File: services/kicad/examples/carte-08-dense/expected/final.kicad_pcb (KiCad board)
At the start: 2 copper layers, 125 x 95 mm, 56 parts, among them J1 IN_5V, J2 SWD, J3 IO0, J4 IO1, J5 IO2, J6 IO3, J7 IO4, U1 STM32F103C8T6, U2 AMS1117-3.3

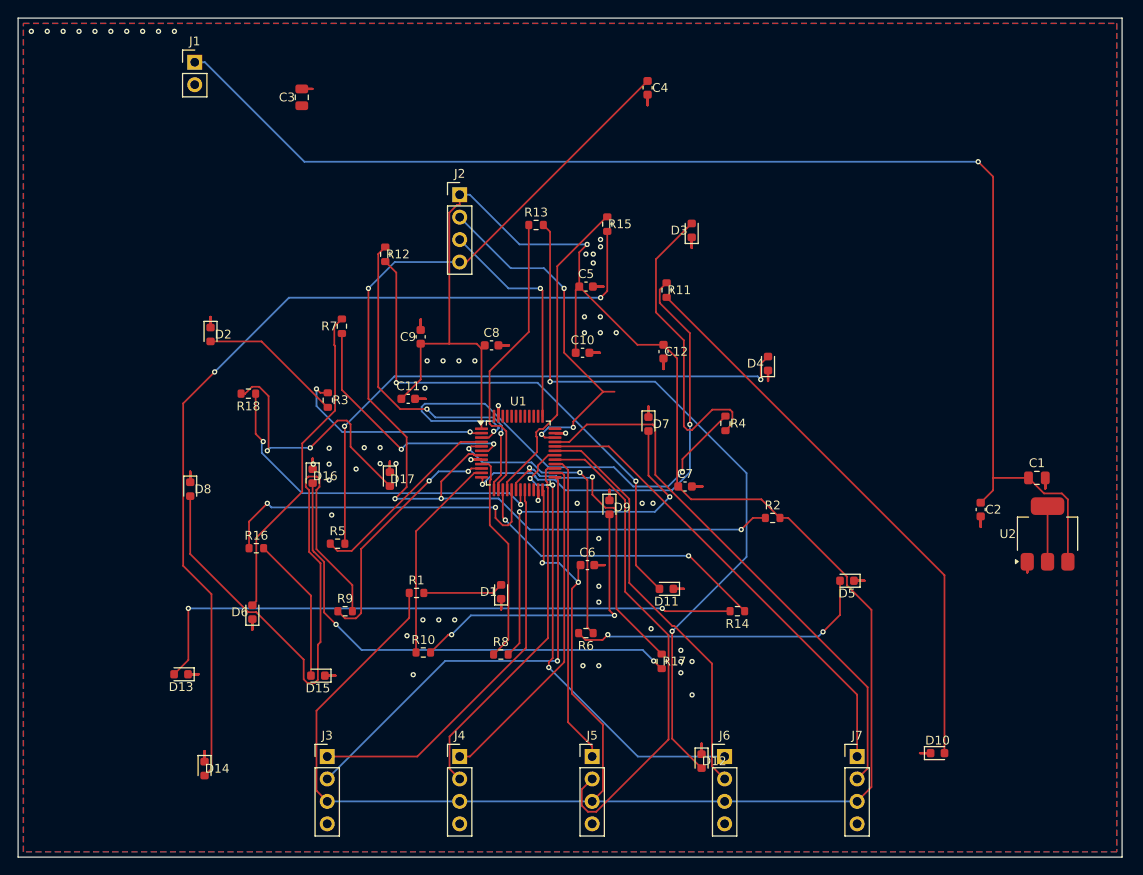
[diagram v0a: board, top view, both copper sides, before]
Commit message: feat(kicad): placement pro et routage 100 % fabricable sur les 16 cartes -- integration sur main (#164)
Branche d'integration coupee depuis origin/main (fab2a82, PR #162) : les
fichiers cles de main etaient des instantanes de feat/placement-seed-snap-
bypass (routing.py = 7981019, placement.py = 437a8b4...). On reprend donc
l'arbre entier de cette branche (345 commits, dernier 9f48667) et on y
conserve ce que main seul apportait :
- tools/verrou_routage.py + son test : « 6,2 Go par routage » rectifie
  (0,2 Go mesure ; c'est la concurrence qui emballe la memoire) ;
- tests/test_driver_llm_resync.py ;
- CLAUDE.md, PLAN.md, DECISIONS.md : fusion a trois voies, les sections
  des deux lignes conservees (2026-09-05 conteneur/verrou, 2026-09-07
  parcours asynchrone et chaine du driver, 2026-09-09/10 lecons).
Les skills *-delegate restent supprimes (remplaces le 2026-08-30).

Contenu : banc en deux phases (placement valide puis routage gele), snap
sur les regles natives, repli GND cible, journal Freerouting incremental,
horloge sans progres, via d'echappement vers le plan principal,
serigraphie degagee ; 16 cartes livrees a 100 %, 0 erreur DRC.

Verification : pytest services/kicad 1805 passed, 16 skipped ;
pnpm type-check 8/8.


Claude-Session: https://claude.ai/code/session_01TnMqm4La2CxQHHB5K8aSSV

Co-authored-by: Claude Fable 5.1 <noreply@anthropic.com>
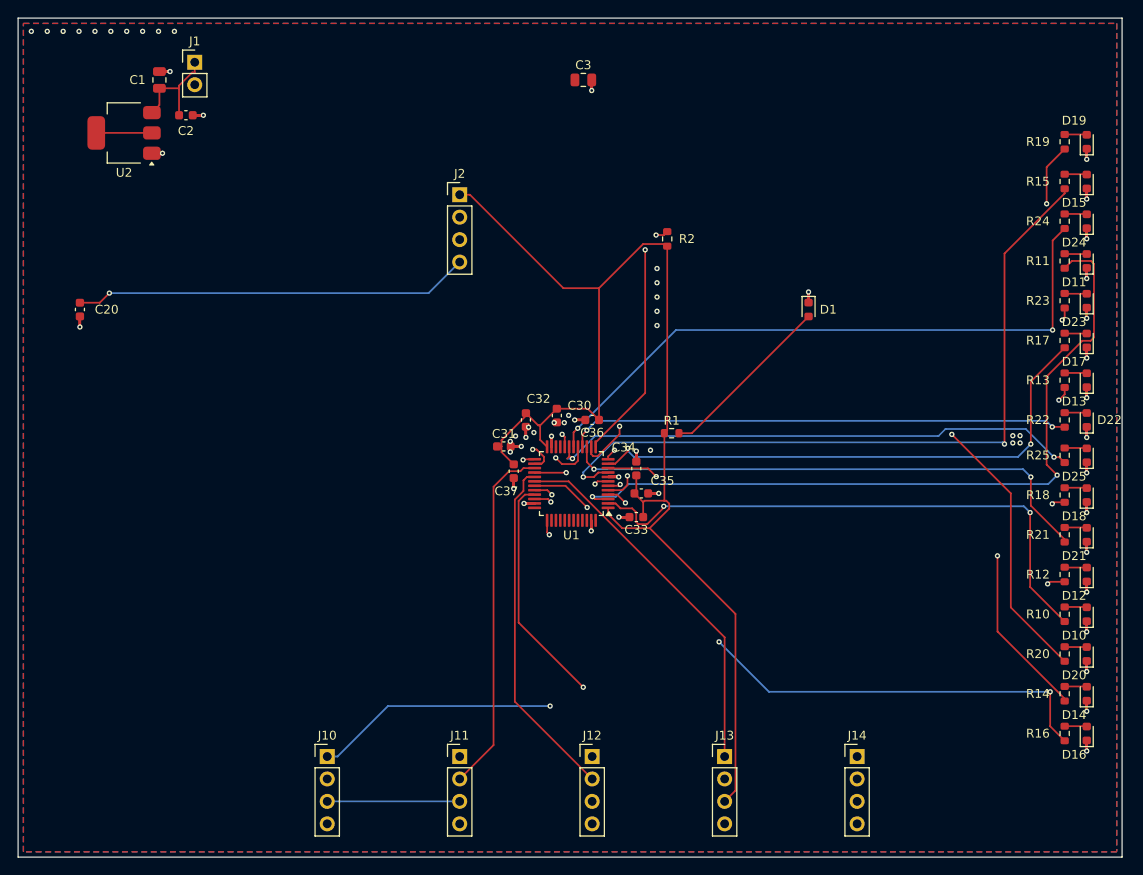
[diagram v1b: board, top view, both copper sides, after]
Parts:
- removed C10, C11, C12, C4, C5, C6, C7, C8, C9: 100nF, C_0603_1608Metric
- removed D2, D3, D4, D5, D6, D7, D8, D9: LED, LED_0603_1608Metric
- removed J3: IO0, PinHeader_1x04_P2.54mm_Vertical
- removed J4: IO1, PinHeader_1x04_P2.54mm_Vertical
- removed J5: IO2, PinHeader_1x04_P2.54mm_Vertical
- removed J6: IO3, PinHeader_1x04_P2.54mm_Vertical
- removed J7: IO4, PinHeader_1x04_P2.54mm_Vertical
- removed R3, R4, R5, R6, R7, R8, R9: 1k, R_0603_1608Metric
- added C20: 100nF, C_0603_1608Metric, F.Cu at (93.0, 90.5)
- added C30: 100nF, C_0603_1608Metric, F.Cu at (147.0, 102.5)
- added C31: 100nF, C_0603_1608Metric, F.Cu at (141.0, 106.0)
- added C32: 100nF, C_0603_1608Metric, F.Cu at (143.5, 103.0)
- added C33: 100nF, C_0603_1608Metric, F.Cu at (156.0, 114.0)
- added C34: 100nF, C_0603_1608Metric, F.Cu at (156.0, 108.5)
- added C35: 100nF, C_0603_1608Metric, F.Cu at (156.6, 111.3)
- added C36: 100nF, C_0603_1608Metric, F.Cu at (151.0, 103.0)
- added C37: 100nF, C_0603_1608Metric, F.Cu at (142.1, 108.8)
- added D18: LED, LED_0603_1608Metric, F.Cu at (207.0, 111.5)
- added D19: LED, LED_0603_1608Metric, F.Cu at (207.0, 71.5)
- added D20: LED, LED_0603_1608Metric, F.Cu at (207.0, 129.5)
- added D21: LED, LED_0603_1608Metric, F.Cu at (207.0, 116.0)
- added D22: LED, LED_0603_1608Metric, F.Cu at (207.0, 103.0)
- added D23: LED, LED_0603_1608Metric, F.Cu at (207.0, 89.5)
- added D24: LED, LED_0603_1608Metric, F.Cu at (207.0, 80.5)
- added D25: LED, LED_0603_1608Metric, F.Cu at (207.0, 107.0)
- added J10: IO0, PinHeader_1x04_P2.54mm_Vertical, F.Cu at (121.0, 141.1)
- added J11: IO1, PinHeader_1x04_P2.54mm_Vertical, F.Cu at (136.0, 141.1)
- added J12: IO2, PinHeader_1x04_P2.54mm_Vertical, F.Cu at (151.0, 141.1)
- added J13: IO3, PinHeader_1x04_P2.54mm_Vertical, F.Cu at (166.0, 141.1)
- added J14: IO4, PinHeader_1x04_P2.54mm_Vertical, F.Cu at (181.0, 141.1)
- added R19: 1k, R_0603_1608Metric, F.Cu at (204.5, 71.5)
- added R20: 1k, R_0603_1608Metric, F.Cu at (204.5, 129.5)
- added R21: 1k, R_0603_1608Metric, F.Cu at (204.5, 116.0)
- added R22: 1k, R_0603_1608Metric, F.Cu at (204.5, 103.0)
- added R23: 1k, R_0603_1608Metric, F.Cu at (204.5, 89.5)
- added R24: 1k, R_0603_1608Metric, F.Cu at (204.5, 80.5)
- added R25: 1k, R_0603_1608Metric, F.Cu at (204.5, 107.0)
- moved U2 114.0 mm to (98.0, 70.5), turned to 180 degrees
- moved C1 109.1 mm to (102.0, 64.5), turned to 90 degrees
- moved D13 107.8 mm to (207.0, 98.5), turned to 90 degrees
- moved D15 103.5 mm to (207.0, 76.0), turned to 90 degrees
- moved C2 100.5 mm to (105.0, 68.5), turned to 0 degrees
- moved D14 100.2 mm to (207.0, 134.0), turned to 90 degrees
- moved R16 93.9 mm to (204.5, 138.5), turned to 90 degrees
- moved R18 93.1 mm to (204.5, 111.5), turned to 90 degrees
- moved D16 92.4 mm to (207.0, 138.5), turned to 90 degrees
- moved R12 85.0 mm to (204.5, 120.5), turned to 90 degrees
- moved D17 80.5 mm to (207.0, 94.0), turned to 90 degrees
- moved R10 72.7 mm to (204.5, 125.0), turned to 90 degrees
- moved R13 62.4 mm to (204.5, 98.5), turned to 90 degrees
- moved D11 60.4 mm to (207.0, 85.0), turned to 90 degrees
- moved R17 58.3 mm to (204.5, 94.0), turned to 90 degrees
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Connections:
- D10 pad 2: LEDA8 -> LEDA0
- D11 pad 2: LEDA9 -> LEDA1
- D12 pad 2: LEDA10 -> LEDA2
- D13 pad 2: LEDA11 -> LEDA3
- D14 pad 2: LEDA12 -> LEDA4
- D15 pad 2: LEDA13 -> LEDA5
- D16 pad 2: LEDA14 -> LEDA6
- D17 pad 2: LEDA15 -> LEDA7
- R10 pad 1: IO_L7 -> IO_L0
- R10 pad 2: LEDA7 -> LEDA0
- R11 pad 1: IO_L8 -> IO_L1
- R11 pad 2: LEDA8 -> LEDA1
- R12 pad 1: IO_L9 -> IO_L2
- R12 pad 2: LEDA9 -> LEDA2
- R13 pad 1: IO_L10 -> IO_L3
- R13 pad 2: LEDA10 -> LEDA3
- R14 pad 1: IO_L11 -> IO_L4
- R14 pad 2: LEDA11 -> LEDA4
- R15 pad 1: IO_L12 -> IO_L5
- R15 pad 2: LEDA12 -> LEDA5
- R16 pad 1: IO_L13 -> IO_L6
- R16 pad 2: LEDA13 -> LEDA6
- R17 pad 1: IO_L14 -> IO_L7
- R17 pad 2: LEDA14 -> LEDA7
- R18 pad 1: IO_L15 -> IO_L8
- R18 pad 2: LEDA15 -> LEDA8
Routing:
- net VIN: track 149.8 -> 12.2 mm, vias 1 -> 0
- net LEDA12: track 103.8 -> 2.52 mm, vias 2 -> 0
- net GND: track 122.4 -> 208.8 mm, vias 58 -> 61
- net LEDA10: track 82.9 -> 2.52 mm, vias 2 -> 0
- net +3V3: track 281.5 -> 208.4 mm, vias 3 -> 0
- net LEDA6: track 70.6 -> 2.52 mm
- net LEDA11: track 69.6 -> 2.52 mm, vias 2 -> 0
- net LEDA2: track 65.9 -> 2.52 mm, vias 2 -> 0
- net LEDA8: track 64.6 -> 2.52 mm
- net IO_L5: track 24.1 -> 84.5 mm, vias 0 -> 2
- net LEDA9: track 59.3 -> 2.52 mm, vias 2 -> 0
- net LEDA14: track 56.1 -> 2.52 mm, vias 2 -> 0
- net IO_L6: track 27.9 -> 73.6 mm, vias 2 -> 3
- net IO_L10: track 33.6 -> 75.1 mm, vias 0 -> 2
- net IO_L0: track 23.4 -> 64.6 mm
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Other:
- copper layers 2 -> 4

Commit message: chore(banc): relivrer carte-01..10 avec la couture corrigee
Boards reroutes par HTTP depuis placement.kicad_pcb inchange, avec le
code de #217. Juges par remesurer_banc.py : 0 erreur, 0 connexion
manquante sur les dix. 678 -> 443 vias ; la rangee de vias GND du bord
haut a disparu.

mesures.json : `board` recompte, `drc_du_board` rejuge, nouvelle cle
`couture_corrigee` (date, vias_avant, couches). journal.txt et les
champs du run d origine sont laisses tels quels et le disent.
rendu-3d.png : kicad-cli, modeles 3D, iso 1400x900.

Couches d un tirage : huit cartes sur 2, carte-08 et carte-10 sur 4.
CLAUDE.md et BANC_DRIVER_LLM.md recomptes. carte-11 non touchee.

Co-Authored-By: Claude Opus 5 (1M context) <noreply@anthropic.com>
Claude-Session: https://claude.ai/code/session_01TnMqm4La2CxQHHB5K8aSSV
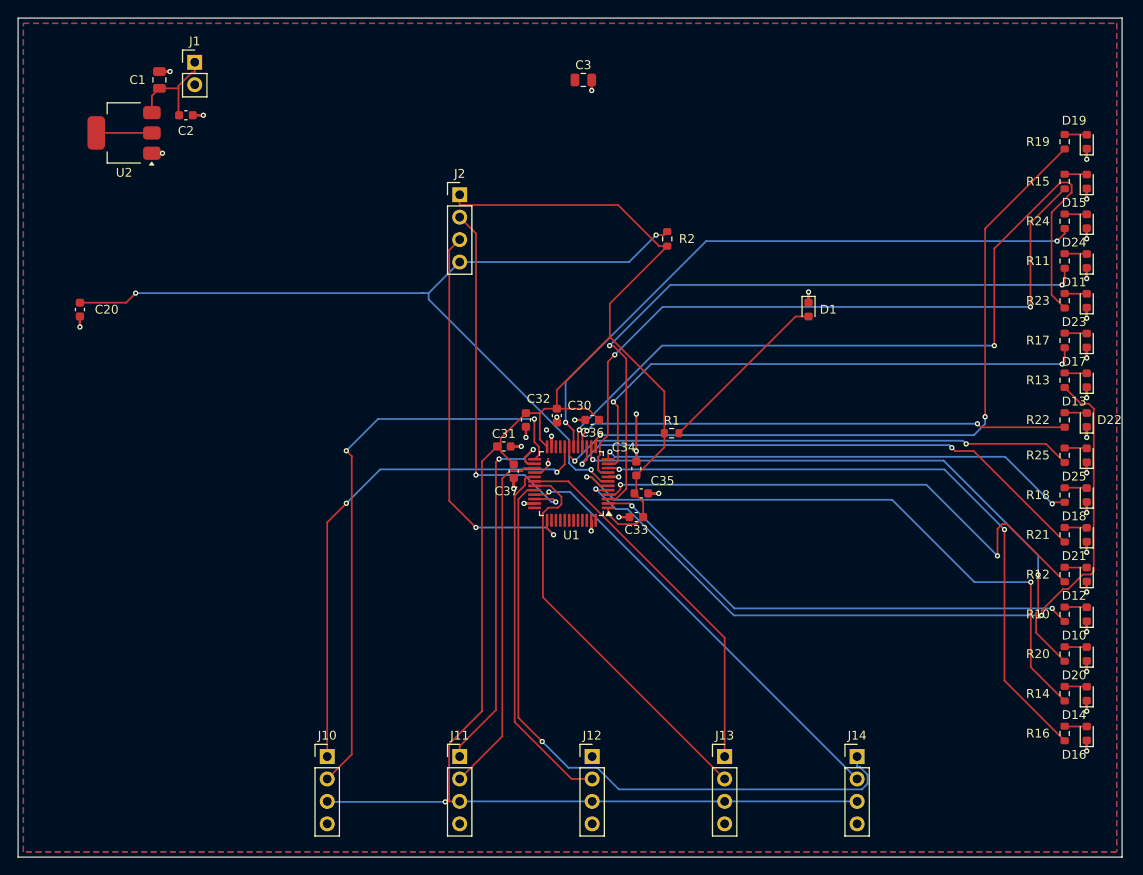
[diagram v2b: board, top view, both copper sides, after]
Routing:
- net GND: track 208.8 -> 90.6 mm, vias 61 -> 36
- net IO_L3: track 62.4 -> 88.9 mm
- net EXT4_1: track 49.0 -> 73.9 mm
- net IO_L13: track 69.8 -> 91.5 mm
- net EXT0_2: track 46.6 -> 66.3 mm, vias 1 -> 2
- net EXT4_2: track 61.6 -> 50.1 mm
- net IO_L1: track 86.5 -> 75.9 mm
- net IO_L0: track 64.6 -> 57.3 mm
- net SWCLK: track 39.4 -> 45.4 mm, vias 1 -> 2
- net IO_L4: track 67.1 -> 73.1 mm
- net IO_L2: track 56.0 -> 61.8 mm
- net IO_L10: track 75.1 -> 69.9 mm
- net IO_L5: track 84.5 -> 79.4 mm
- net +3V3: track 208.4 -> 204.1 mm, vias 0 -> 1
- net SWDIO: track 38.5 -> 42.8 mm, vias 1 -> 2
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
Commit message: fix(kicad): plan de masse referme — banc DIX cartes sur dix, 0 erreur 0 manquante (#237)
* docs(kicad): la derniere rupture de plan tient a UN segment, pas a un faisceau

Diagnostic complet du seul defaut restant du banc (carte-10), mesure sur le
board qui le porte vraiment, apres consultation de Codex et de GLM.

Mesures sur `/tmp/livr/carte-10-maximale/route.kicad_pcb` (33 violations,
0 erreur, 1 connexion manquante) :

- 23 ilots GND sur les deux faces, exactement 2 orphelins, et ce sont des
  JUMEAUX : F.Cu 1,30 mm2 (porte la pastille C35.2) et B.Cu 0,99 mm2.
- AUCUN de leurs points n a le plan principal en vis-a-vis : ils se font face
  l un l autre. La piste « changer de face par un via », proposee par GLM, est
  donc REFUTEE par la mesure.
- La couture de production visite les deux ilots et refuse la totalite de
  leurs sites (23 et 18 candidats ; obstacle 16/10, hors_polygone 6/7,
  trou_trop_pres 1/1) : un via ne tient pas dans un millimetre carre.
  Le raccord par courte piste rend relies 0, sans_chemin 19.
- Mais le plan principal n est qu a 0,862 mm sur F.Cu et 0,781 mm sur B.Cu, et
  UN SEUL segment coupe le couloir de chaque face (EXT2_1, EXT4_1).

Le plan de Codex — deplacer l obstacle au lieu de chercher un passage a
travers — a donc ici un ensemble a arracher d UN segment par face, pas une
recherche ouverte. Decision de strategie de routage : D-2026-09-22-a, EN
ATTENTE. Rien n est implemente.

Levier natif verifie et jamais appele : LocalRerouter.reroute_segment() de
kicad-tools, utilise par drc/repair_clearance.py, zero appelant Cirqix. Il
travaille sur le document S-expression quand notre code travaille sur pcbnew.

Lecons inscrites dans CLAUDE.md :
- j ai d abord mesure le board VERSIONNE du 21, qui est propre (non_connectes
  0) et se pretait a toutes les demonstrations — un via y tenait avec 0,29 mm
  de marge. Verifier que l artefact PORTE le defaut avant de le diagnostiquer.
- ma premiere sonde raisonnait zone par zone, alors que la carte por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
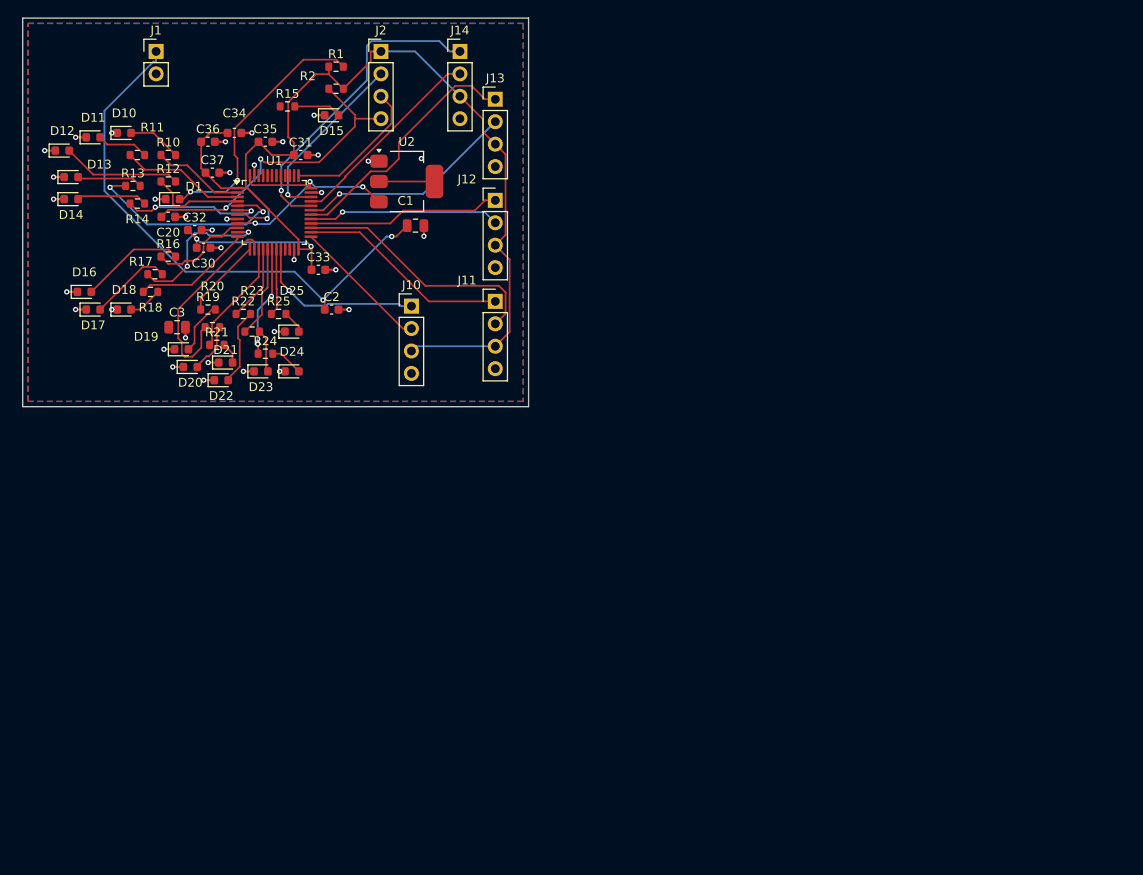
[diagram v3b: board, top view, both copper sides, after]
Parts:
- moved D14 127.9 mm to (92.0, 78.0), turned to 0 degrees
- moved D12 125.5 mm to (91.0, 72.5), turned to 0 degrees
- moved D16 124.0 mm to (93.5, 88.5), turned to 0 degrees
- moved D10 121.9 mm to (98.0, 70.5), turned to 0 degrees
- moved R14 118.8 mm to (99.5, 78.5), turned to 0 degrees
- moved D13 117.3 mm to (92.0, 75.5), turned to 0 degrees
- moved R16 115.0 mm to (103.0, 84.5), turned to 0 degrees
- moved R10 114.0 mm to (103.0, 73.0), turned to 0 degrees
- moved D11 113.4 mm to (94.5, 71.0), turned to 0 degrees
- moved D17 112.6 mm to (94.5, 90.5), turned to 0 degrees
- moved D18 111.0 mm to (98.0, 90.5), turned to 0 degrees
- moved R12 110.8 mm to (103.0, 76.0), turned to 0 degrees
- moved R13 107.8 mm to (99.0, 76.5), turned to 0 degrees
- moved D20 106.6 mm to (105.5, 97.0), turned to 0 degrees
- moved R18 106.0 mm to (101.0, 88.5), turned to 0 degrees
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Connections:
- U1 pad 36: Net-(U1-36) -> PWR_FLAG
- U1 pad 48: Net-(U1-48) -> PWR_FLAG
- U1 pad 9: IO_L5 -> PWR_FLAG
- U2 pad 3: VIN -> PWR_FLAG
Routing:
- net IO_L13: track 91.5 -> 10.4 mm, vias 2 -> 0
- net IO_L5: track 79.4 -> 0.00 mm, vias 2 -> 0
- net +3V3: track 204.1 -> 127.2 mm, vias 1 -> 2
- net IO_L9: track 80.5 -> 9.15 mm, vias 2 -> 0
- net IO_L3: track 88.9 -> 24.7 mm
- net IO_L6: track 74.5 -> 11.3 mm, vias 2 -> 0
- net IO_L1: track 75.9 -> 14.1 mm, vias 2 -> 0
- net IO_L14: track 71.8 -> 12.5 mm
- net NRST: track 101.1 -> 44.1 mm
- net IO_L4: track 73.1 -> 16.2 mm
- net IO_L15: track 59.3 -> 7.61 mm, vias 2 -> 0
- net GND: track 90.6 -> 39.0 mm, vias 36 -> 35
- net IO_L2: track 61.8 -> 10.7 mm, vias 2 -> 0
- net EXT0_2: track 66.3 -> 15.7 mm, vias 2 -> 0
- net VIN: track 12.2 -> 62.4 mm, vias 0 -> 2
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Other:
- board size 125 x 95 mm -> 57.3 x 44 mm
- copper layers 4 -> 2
